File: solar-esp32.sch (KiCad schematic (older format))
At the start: 34 parts, among them J1 Solar, J2 BAT+, J3 BAT-, J4 ESP32, Q1 DMP1045U-7, Q2 SSM3J332RLF, U1 CN3801, U2 NCP302HSN30

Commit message: Replaced active-high supervisor and p-channel mosfet with an active-low supervisor connected to EN (enable) pin on ESP32.
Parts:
- removed C8, C9: 100nF, Capacitor_SMD:C_1206_3216Metric_Pad1.33x1.80mm_HandSolder, symbol Device:C
- removed D5: D_Zener, Diode_SMD:D_SOD-123, symbol Device:D_Zener
- removed J3: BAT-, Connector_PinHeader_2.54mm:PinHeader_1x02_P2.54mm_Vertical, symbol Connector:Conn_01x02_Male
- removed Q2: SSM3J332RLF, Package_TO_SOT_SMD:SOT-23, symbol Transistor_FET:AO3401A
- removed R6: 10k, Resistor_SMD:R_1206_3216Metric_Pad1.30x1.75mm_HandSolder, symbol Device:R
- removed U2: NCP302HSN30, Package_TO_SOT_SMD:SOT-23-5, symbol 0xFD:NCP302HSN30
- added R10: 100k, Resistor_SMD:R_1206_3216Metric_Pad1.30x1.75mm_HandSolder, symbol Device:R
- added U2: APX803L, Package_TO_SOT_SMD:SOT-23, symbol Power_Supervisor:LM809
- J2: value BAT+ -> BAT
- J4: footprint Connector_PinHeader_2.54mm:PinHeader_1x04_P2.54mm_Vertical -> Connector_PinHeader_2.54mm:PinHeader_1x06_P2.54mm_Vertical; symbol Connector:Conn_01x04_Female -> Connector:Conn_01x06_Female
- renumbered C10 to C8
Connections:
- net labels added: EN
- net labels removed: Cd, ESP-LOAD, LVCO
- wire segments 133 -> 119
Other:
- moved on the sheet: J2, R9

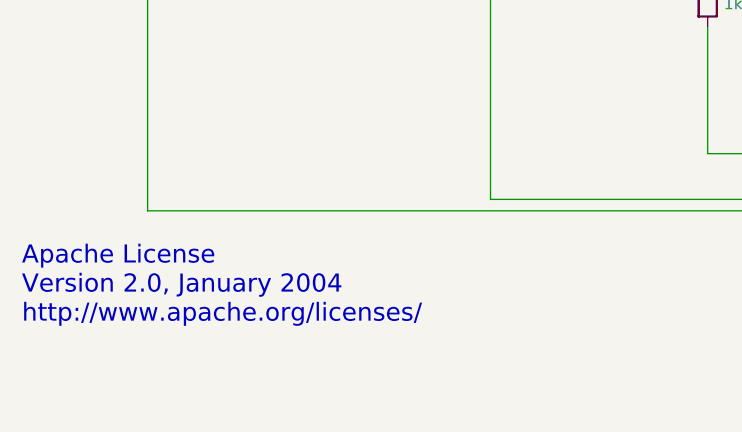
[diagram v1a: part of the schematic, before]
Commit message: Changed to BSD 2.0 license, and added OpenHardware logo
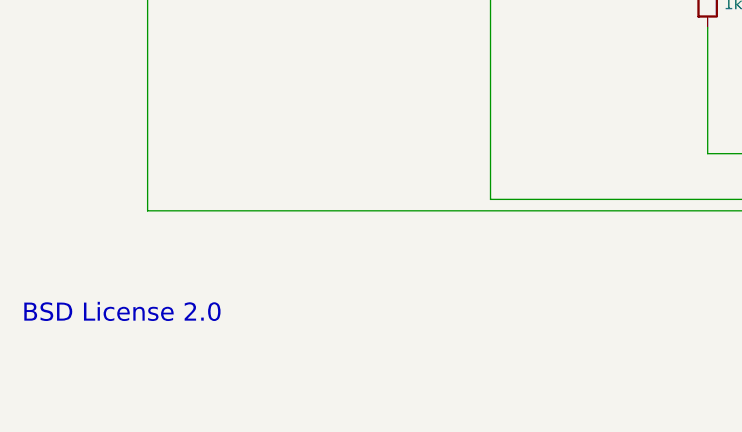
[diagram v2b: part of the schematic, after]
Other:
- note added: "BSD License 2.0"
- note removed: "Apache License\nVersion 2.0, January 2004\nhttp://www.apache.org/licenses/"
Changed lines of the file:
@@
 MPPT
 Text Notes 650  7600 0    79   ~ 0
-Apache License\nVersion 2.0, January 2004\nhttp://www.apache.org/licenses/
+BSD License 2.0
 Wire Wire Line
 	1850 1250 2200 1250

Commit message: Added 100uF capacitor near active-low supervisor.
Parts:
- added C9: 100uF, Capacitor_SMD:C_1206_3216Metric_Pad1.33x1.80mm_HandSolder, symbol Device:C
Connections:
- wire segments 119 -> 123
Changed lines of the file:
@@
 	5050 3550 6150 3550
 Wire Wire Line
-	5850 2400 5850 4250
+	5850 2400 5850 3900
 Wire Wire Line
 	5500 4450 5850 4450
@@
 	4700 4450 4500 4450
 Wire Wire Line
-	4500 4450 4500 3550
+	4500 4450 4500 3900
 Connection ~ 4500 3550
 Wire Wire Line
@@
 Wire Wire Line
 	5850 4250 5850 4450
+$Comp
+L Device:C C9
+U 1 1 607CCEC6
+P 5500 3900
+F 0 "C9" V 5272 3900 50  0000 C CNN
+F 1 "100uF" V 5363 3900 50  0000 C CNN
+F 2 "Capacitor_SMD:C_1206_3216Metric_Pad1.33x1.80mm_HandSolder" H 5538 3750 50  0001 C CNN
+F 3 "~" H 5500 3900 50  0001 C CNN
+	1    5500 3900
+	0    1    -1   0
+$EndComp
+Wire Wire Line
+	5350 3900 4500 3900
+Connection ~ 4500 3900
+Wire Wire Line
+	4500 3900 4500 3550
+Wire Wire Line
+	5650 3900 5850 3900
+Connection ~ 5850 3900
+Wire Wire Line
+	5850 3900 5850 4250
 $EndSCHEMATC
